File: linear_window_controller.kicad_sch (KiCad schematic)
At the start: 85 parts, among them J1 Motor 2, J2 Motor 1, J3 Motor 4, J4 Motor 3, J5 edge_psu_connector_64p, J9 Control, P1 ESP32 USB, SW2 Service, SW3 Service, SW4 Service, SW5 Service, SW6 Service, SW7 Service, U1 TSOP384xx, U10 TPS56220x, U2 DRV8874, U3 DRV8874, U4 DRV8874, U5 DRV8874, U6 PCF8574APWRG4, U8 ESP32-S3-WROOM-1-N16R2

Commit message: Finish most of the routing, add DM9051 fast ethernet controller
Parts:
- removed DS2: OLED-128O064D, iotta_footprints:OLED_0.96'_SSD1306_Folded, symbol Display_Graphic:OLED-128O064D
- added C20, C22, C27, C28, C33, C35: 22u, Capacitor_SMD:C_0603_1608Metric, symbol Device:C
- added C21, C23, C24, C26, C29, C30, C31, C32, C34, C36, C37, C45, C46: 100n, Capacitor_SMD:C_0603_1608Metric, symbol Device:C
- added C47: 1u, Capacitor_SMD:C_0603_1608Metric, symbol Device:C
- added D3, D4, D5, D8: SS14, Diode_SMD:D_SMA, symbol Diode:SS14
- added D6, D7: LED, LED_SMD:LED_0603_1608Metric, symbol Device:LED
- added DIS1: OLED_128x64, iotta_footprints:OLED_128x64_Module, symbol iotta:OLED_128x64
- added J6: ATX-24 (Molex 39-28-1243), Connector_Molex:Molex_Mini-Fit_Jr_5566-24A_2x12_P4.20mm_Vertical, symbol Connector:ATX-24
- added J7: Link-PP_LPJ0135GDNL, iotta_footprints:LinkPP_LPJ0135GDNL, symbol iotta:Link-PP_LPJ0135GDNL
- added J8: EXT_LED, Connector_PinSocket_2.54mm:PinSocket_1x03_P2.54mm_Vertical, symbol Connector_Generic:Conn_01x03
- added L2: FB0805/600R/2A, symbol Device:L_Ferrite_Small
- added P2: ESP32 USB, Connector_USB:USB_C_Receptacle_Palconn_UTC16-G, symbol Connector:USB_C_Receptacle_USB2.0_14P
- added Q1, Q2: BC817-40(SOT23), Package_TO_SOT_SMD:SOT-23, symbol MicroGw_prj:Q_NPN_BEC
- added Q3: BSS138, Package_TO_SOT_SMD:SOT-23, symbol Transistor_FET:BSS138
- added R27: 0, Resistor_SMD:R_0603_1608Metric, symbol Device:R
- added R28, R31, R32: 1k, Resistor_SMD:R_0603_1608Metric, symbol MicroGw_prj:R
- added R29, R30: 220, Resistor_SMD:R_0603_1608Metric, symbol MicroGw_prj:R
- added R33, R45, R46, R47, R48, R49, R50: 10k, Resistor_SMD:R_0603_1608Metric, symbol Device:R
- added R34: 100, Resistor_SMD:R_0603_1608Metric, symbol MicroGw_prj:R
- added R35, R36: 100, Resistor_SMD:R_0603_1608Metric, symbol Device:R
- added R37: 6k8, Resistor_SMD:R_0603_1608Metric, symbol Device:R
- added R38, R39, R44, R51: 300, Resistor_SMD:R_0603_1608Metric, symbol Device:R
- added R40, R41, R42, R43: 49.9, Resistor_SMD:R_0603_1608Metric, symbol Device:R
- added SW1: PGM, Button_Switch_SMD:SW_SPST_B3U-1000P, symbol Switch:SW_Push
- added U11: CP2102N-A01-GQFN24, Package_DFN_QFN:QFN-24-1EP_4x4mm_P0.5mm_EP2.6x2.6mm, symbol Interface_USB:CP2102N-A01-GQFN24
- added U12: 93LCxxAxxOT, Package_TO_SOT_SMD:SOT-23-6, symbol Memory_EEPROM:93LCxxAxxOT
- added U13: DM9051, Package_DFN_QFN:QFN-32-1EP_5x5mm_P0.5mm_EP3.3x3.3mm_ThermalVias, symbol iotta_v6:DM9051
- added Y1: 25MHz YXC X322525MOB4SI, Crystal:Crystal_SMD_3225-4Pin_3.2x2.5mm, symbol Device:Crystal_GND24
- F1: footprint Fuse:Fuseholder_Cylinder-5x20mm_Schurter_0031_8201_Horizontal_Open -> Fuse:Fuseholder_Clip-6.3x32mm_Littelfuse_102_122_Inline_P34.21x7.62mm_D1.98mm_Horizontal
- J5: value edge_psu_connector_64p -> Amphenol 10053363-200LF; footprint iotta_footprints_v6:Amphenol_10053363-200LF_WingTAT ER64BGFBK_Compatible -> iotta_footprints_v6:Amphenol_10053363-200LF_WingTAT ER64BGFBK_Compatible_BOTTOM
- P1: symbol Connector:USB_C_Plug_USB2.0 -> Connector:USB_C_Receptacle_USB2.0_14P
- SW6: now not fitted
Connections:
- net +12V_UNFUSED: now also J6.10 (+12V), J6.11 (+12V)
- net +3.3V: now also D1.2 (A), D2.2 (A), U1.3 (Vs), C26.2, C27.2, C28.2, C29.2, C30.2, C31.2, DIS1.2 (GND), J8.2 (Pin_2), L2.1, R33.2, R38.2, R39.2, R44.2, R45.2, R47.2, R48.2, R49.2, U12.6 (VCC), U13.15 (VDD33), U13.21 (VDD33), U13.29 (VDD33), U13.9 (TEST3); no longer R2.2, R3.2
- net A_DWN: now also SW5.2, U6.17 (P5); no longer SW3.2, U6.19 (P6)
- net A_UP: now also SW4.2, U6.16 (P4); no longer SW2.2, U6.20 (P7)
- net BTN_FUNC: now also U6.10 (P0); no longer U6.12 (P2)
- net B_DWN: now also SW3.2, U6.20 (P7); no longer SW5.2, U6.17 (P5)
- net B_UP: now also SW2.2, U6.19 (P6); no longer SW4.2, U6.16 (P4)
- net DRV1_IN1: now also U8.29 (SPIIO7/GPIO36/FSPICLK/SUBSPICLK)
- net DRV1_IN2: now also U8.28 (SPIIO6/GPIO35/FSPID/SUBSPID)
- net DRV1_IPROPI: now also U8.39 (GPIO1/TOUCH1/ADC1_CH0)
- net DRV2_IN1: now also U8.24 (GPIO47/SPICLK_P/SUBSPICLK_P_DIFF)
- net DRV2_IN2: now also U8.23 (GPIO21)
- net DRV2_IPROPI: now also U8.18 (GPIO10/TOUCH10/ADC1_CH9/FSPICS0/FSPIIO4/SUBSPICS0)
- net DRV3_IN1: now also U8.19 (GPIO11/TOUCH11/ADC2_CH0/FSPID/FSPIIO5/SUBSPID)
- net DRV3_IN2: now also U8.20 (GPIO12/TOUCH12/ADC2_CH1/FSPICLK/FSPIIO6/SUBSPICLK)
- net DRV3_IPROPI: now also U8.17 (GPIO9/TOUCH9/ADC1_CH8/FSPIHD/SUBSPIHD)
- net DRV4_IN1: now also U8.10 (GPIO17/U1TXD/ADC2_CH6)
- net DRV4_IN2: now also U8.11 (GPIO18/U1RXD/ADC2_CH7/CLK_OUT3)
- net DRV4_IPROPI: now also U8.15 (GPIO3/TOUCH3/ADC1_CH2)
- net GND: now also P1.A1 (GND), P1.A12 (GND), P1.B1 (GND), P1.B12 (GND), P1.S1 (SHIELD), U1.2 (GND), U8.1 (GND), U8.40 (GND), U8.41 (GND), C20.2, C21.2, C22.2, C23.2, C24.2, C26.1, C27.1, C28.1, C29.1, C30.1, C31.1, C32.1, C33.1, C34.1, C35.2, C36.1, C37.1, C45.2, C46.2, C47.2, DIS1.1 (VCC), J6.15 (GND), J6.17 (GND), J6.18 (GND), J6.19 (GND), J6.24 (GND), J6.3 (GND), J6.5 (GND), J6.7 (GND), P2.A1 (GND), P2.A12 (GND), P2.B1 (GND), P2.B12 (GND), P2.S1 (SHIELD), Q3.2 (S), R27.2, R37.2, R46.2, R50.1, R51.2, SW1.1, U11.2 (GND), U11.25 (GND), U12.2 (GND), U13.22 (TEST2), U13.32 (AGND), U13.33 (VSS), U13.5 (AGND), Y1.2, Y1.4; no longer J5.A27 (ADDR)
- net LED_F1: now also R3.1, U6.11 (P1), R35.2; no longer D1.1 (K), U6.10 (P0)
- net LED_F2: now also R2.1, U6.12 (P2), R36.2; no longer D2.1 (K), U6.11 (P1)
- net PS_OK: now also D7.2 (A), J6.8 (PWR_OK)
- net PS_ON: now also J6.16 (PS_ON#), Q3.3 (D)
- net SCL: now also U8.8 (GPIO15/U0RTS/ADC2_CH4/XTAL_32K_P), DIS1.3 (SCL), R48.1
- net SDA: now also U8.9 (GPIO16/U0CTS/ADC2_CH5/XTAL_32K_N), DIS1.4 (SDA), R49.1
- net ~{DRV1_FAULT}: now also U8.25 (GPIO48/SPICLK_N/SUBSPICLK_N_DIFF)
- net ~{DRV2_FAULT}: now also U8.22 (GPIO14/TOUCH14/ADC2_CH3/FSPIWP/FSPIDQS/SUBSPIWP)
- net ~{DRV3_FAULT}: now also U8.21 (GPIO13/TOUCH13/ADC2_CH2/FSPIQ/FSPIIO7/SUBSPIQ)
- net ~{DRV4_FAULT}: now also U8.12 (GPIO8/TOUCH8/ADC1_CH7/SUBSPICS1)
- net ~{DRV_SLEEP}: now also U8.26 (GPIO45)
- net ESPUSB-: now reaches U8.13 (GPIO19/U1RTS/ADC2_CH8/CLK_OUT2/USB_D-)
- net ESPUSB-: now also P1.A7 (D-), P1.B7 (D-)
- net ESPUSB+: now reaches U8.14 (GPIO20/U1CTS/ADC2_CH9/CLK_OUT1/USB_D+)
- net ESPUSB+: now also P1.A6 (D+), P1.B6 (D+)
- net ~{IOEX1_INT}: now reaches U8.16 (GPIO46)
- net ~{IOEX1_INT}: now also U6.1 (~{INT})
- net ~{ESP_PGM}: now reaches U8.27 (GPIO0/BOOT)
- net ~{ESP_PGM}: now also R34.1
- net ESP_EN: now reaches U8.3 (EN)
- net ESP_EN: now also C24.1, Q1.3 (C), R33.1
- net LAN_MISO: now reaches U8.30 (SPIDQS/GPIO37/FSPIQ/SUBSPIQ)
- net LAN_MISO: now also U13.20 (SPI_MISO)
- net LAN_MOSI: now reaches U8.31 (GPIO38/FSPIWP/SUBSPIWP)
- net LAN_MOSI: now also U13.19 (SPI_MOSI)
- net LAN_CK: now reaches U8.32 (MTCK/GPIO39/CLK_OUT3/SUBSPICS1)
- net LAN_CK: now also U13.18 (SPI_CK)
- net LAN_CSN: now reaches U8.33 (MTDO/GPIO40/CLK_OUT2)
- net LAN_CSN: now also U13.17 (SPI_CSN)
- net ~{LAN_INT}: now reaches U8.34 (MTDI/GPIO41/CLK_OUT1)
- net ~{LAN_INT}: now also U13.24 (INT)
- net IR_REMOTE: now reaches U8.35 (MTMS/GPIO42)
- net IR_REMOTE: now also U1.1 (OUT)
- net U0RXD: now reaches U8.36 (U0RXD/GPIO44/CLK_OUT2)
- net U0RXD: now also R30.2
- net U0TXD: now reaches U8.37 (U0TXD/GPIO43/CLK_OUT1)
- net U0TXD: now also R29.2
- net PS_ENABLE: now reaches U8.38 (GPIO2/TOUCH2/ADC1_CH1)
- net PS_ENABLE: now also Q3.1 (G), R50.2
- net at P1.A4 (VBUS), P1.A9 (VBUS), P1.B4 (VBUS)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: now also D4.2 (A)
- net +12P renamed DCDC_IN
- net DCDC_IN: now also D3.1 (K), D4.1 (K), D5.1 (K), D8.1 (K); no longer J5.B28 (+12VSB), R1.2
- new net: C20.1, C21.1, R28.1, U11.5 (VIO), U11.6 (VDD)
- new net: R28.2, U11.9 (~{RSTb})
- new net: Q2.3 (C), R34.2, SW1.2
- new net: C36.2, U13.30 (X2), Y1.1
- new net: C37.2, U13.31 (X1), Y1.3
- new net: C46.1, R42.1, R43.1
- new net: D2.1 (K), R2.2
- new net: J7.1 (RD+), R40.2, U13.3 (RX+)
- new net: J7.11 (LED1_A), R38.1
- new net: J7.13 (LED2_A), R39.1
- new net: J7.3 (RD-), R41.2, U13.4 (RX-)
- new net: J7.4 (TD+), R42.2, U13.6 (TX+)
- new net: J7.6 (TD-), R43.2, U13.7 (TX-)
- new net: Q2.1 (B), R32.2
- new net: R37.1, U13.1 (BGRES)
- new net: R46.1, U13.14 (WOL)
- new net: C45.1, R40.1, R41.1
- new net: C47.1, R47.1, U13.27 (RSTB)
- new net: D7.1 (K), R51.1
- new net: D6.2 (A), R44.1
- new net: D1.1 (K), R3.2
- new net: J5.A27 (ADDR), R27.1
- new net: J8.3 (Pin_3), R36.1
- new net: Q1.1 (B), R31.2
- new net: J8.1 (Pin_1), R35.1
- new net +3.3v: J6.1 (+3.3V), J6.12 (+3.3V), J6.13 (+3.3V), J6.2 (+3.3V)
- new net +5VSB: D8.2 (A), J6.9 (+5VSB)
- new net +5v: J6.21 (+5V), J6.22 (+5V), J6.23 (+5V), J6.4 (+5V), J6.6 (+5V)
- new net +V12SB: D3.2 (A), J5.B28 (+12VSB), R1.2
- new net -12V: J6.14 (-12V)
- new net AVDD: C32.2, C33.2, C34.2, C35.1, J7.2 (CT), J7.5 (CT), L2.2, U13.2 (AVDD), U13.8 (AVDD)
- new net DTR: Q2.2 (E), R31.1, U11.23 (DTR)
- new net EECK: R45.1, U12.4 (CLK), U13.12 (EECK)
- new net EECS: U12.5 (CS), U13.13 (EECS)
- new net EEDIO: U12.1 (DO), U12.3 (DI), U13.11 (EEDIO)
- new net LAN_ACT: J7.12 (LED1_K), U13.25 (LINKLED)
- new net LAN_FDX: D6.1 (K), U13.16 (FXLED)
- new net LAN_SPEED: J7.14 (LED2_K), U13.26 (SPDLED)
- new net RTS: Q1.2 (E), R32.1, U11.19 (RTS)
- new net RXD: R29.1, U11.20 (RXD)
- new net TXD: R30.1, U11.21 (TXD)
- new net USB_D+: P2.A6 (D+), P2.B6 (D+), U11.3 (D+)
- new net USB_D-: P2.A7 (D-), P2.B7 (D-), U11.4 (D-)
- new net VBUS: C22.1, C23.1, D5.2 (A), P2.A4 (VBUS), P2.A9 (VBUS), P2.B4 (VBUS), P2.B9 (VBUS), U11.7 (REGIN), U11.8 (VBUS)
- no-connect marks 0 -> 13
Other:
- note added: "0"
- note added: "1"
- note added: "1.8V"
- note added: "3.3V"
- note added: "Auto program"
- note added: "Booting Mode"
- note added: "Bootstrapping Pins Settings"
- note added: "DTR RTS->EN IO0"
- note added: "Debugging Log on U0TXD During Booting"
- note added: "Default"
- note added: "Don't-care"
- note added: "Download Boot"
- note added: "EECK strap: INT low active"
- note added: "Falling-edge:Input"
- note added: "Falling-edge:Output"
- note added: "GPIO0"
- note added: "GPIO0:"
- note added: "GPIO12/MTDI"
- note added: "GPIO15/MTDO"
- note added: "GPIO2"
- note added: "GPIO2:"
- note added: "GPIO4:"
- note added: "GPIO5"
- note added: "GPIO5:"
- note added: "Internal Bootstrapping Resistors"
- note added: "MTDI/GPIO12:"
- note added: "MTDO/GPIO15:"
- note added: "Pin"
- note added: "Pull-Down"
- note added: "Pull-Up"
- note added: "Rising-edge:Input"
- note added: "Rising-edge:Output"
- note added: "SPI Flash Boot"
- note added: "Timing of SDIO Slave"
- note added: "U0TXD Silent"
- note added: "U0TXD Toggling"
- note added: "VCC/GND POLARISATIONS BOTH EXIST"
- note added: "Voltage of Internal LDO(VDD_SDIO)"
- note added: "WOL strap: INT Push-Pull"
- moved on the sheet: C17, C42, C43, C47, D1, D2, J9, L6, R2, R24, R3, R6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

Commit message: Finalize routing and cleanup. Change DCDC to TPS562200 Add some more things (e.g. power monitoring LEDs) Update some partno's in BOM
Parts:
- removed U10: TPS56220x, Package_TO_SOT_SMD:SOT-23-6, symbol iotta_v6:TPS56220x
- added D10: Vsb, LED_SMD:LED_0603_1608Metric, symbol Device:LED
- added D11: VCC, LED_SMD:LED_0603_1608Metric, symbol Device:LED
- added D9: Vmain, LED_SMD:LED_0603_1608Metric, symbol Device:LED
- added J10, J11: DCDC_IN, Connector_PinHeader_2.54mm:PinHeader_1x01_P2.54mm_Vertical, symbol Connector:Conn_01x01_Pin
- added J12: VCC, Connector_PinHeader_2.54mm:PinHeader_1x01_P2.54mm_Vertical, symbol Connector:Conn_01x01_Pin
- added J14: PANEL_BTN, Connector_PinHeader_2.54mm:PinHeader_1x06_P2.54mm_Vertical, symbol Connector_Generic:Conn_01x06
- added R52, R53: 1k, Resistor_SMD:R_0603_1608Metric, symbol MicroGw_prj:R
- added R54: 300, Resistor_SMD:R_0603_1608Metric, symbol Device:R
- added R55: 470, Resistor_SMD:R_0603_1608Metric, symbol Device:R
- added R56: 100, Resistor_SMD:R_0603_1608Metric, symbol Device:R
- added U9: TPS562200, Package_TO_SOT_SMD:SOT-23-6, symbol Regulator_Switching:TPS562200
- C36, C37: value 100n -> 18p
- D7: value LED -> PSOK
- J5: LCSC# (none) -> C5173350
- J6: LCSC# (none) -> C114088
- J8: value EXT_LED -> PANEL_LED
- L2: footprint (none) -> Inductor_SMD:L_0805_2012Metric
- L6: value 4.7µ -> 2.2µ; LCSC (none) -> C135262; Manuf (none) -> SXN; PartNr (none) -> SMNR4020-2.2UH
- P1: LCSC# (none) -> C2927039; Manuf (none) -> DEALON; PartNr (none) -> USB-TYPE-C-019
- P2: value ESP32 USB -> CONSOLE; LCSC# (none) -> C2927039; Manuf (none) -> DEALON; PartNr (none) -> USB-TYPE-C-019
- R24: value 100k -> 33k
- R24: value 22k -> 10k
- U12: value 93LCxxAxxOT -> 93LC46BT-E/OT
- Y1: LCSC# (none) -> C9006
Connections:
- net POT+ is gone; now on net +3.3V: J1.5 (Pin_5), J2.5 (Pin_5), J3.5 (Pin_5), J4.5 (Pin_5)
- net POTCOM is gone; now on net GND: J1.3 (Pin_3), J2.3 (Pin_3), J3.3 (Pin_3), J4.3 (Pin_3)
- net +12V_UNFUSED: now also D9.2 (A)
- net +3.3V: now also D11.2 (A), J12.1 (Pin_1)
- net A_DWN: now also J14.3 (Pin_3)
- net A_UP: now also J14.1 (Pin_1)
- net BTN_FUNC: now also U6.14 (P3); no longer U6.10 (P0)
- net BTN_SVC: now also U6.10 (P0); no longer U6.14 (P3)
- net B_DWN: now also J14.6 (Pin_6)
- net B_UP: now also J14.4 (Pin_4)
- net DCDC_IN: now also D10.2 (A), J10.1 (Pin_1), U9.3 (VIN); no longer D4.1 (K)
- net GND: now also J14.2 (Pin_2), J14.5 (Pin_5), R52.2, R53.2, R54.2, R55.2, R56.2, U9.1 (GND)
- net at R6.2: now also U9.5 (EN)
- net at C42.2, L6.1: now also U9.2 (SW)
- net at C42.1: now also U9.6 (VBST)
- net at R24.2, R24.2: now also U9.4 (VFB)
- net at P2.A5 (CC1): now also P2.B5 (CC2), R52.1
- net at P1.A5 (CC1): now also P1.B5 (CC2), R53.1
- net +3.3v: no longer names the net of J6.1 (+3.3V), J6.12 (+3.3V), J6.13 (+3.3V), J6.2 (+3.3V)
- net +5v: no longer names the net of J6.21 (+5V), J6.22 (+5V), J6.23 (+5V), J6.4 (+5V), J6.6 (+5V)
- net -12V: no longer names the net of J6.14 (-12V)
- new net: D9.1 (K), R54.1
- new net: D4.1 (K), J11.1 (Pin_1)
- new net: D11.1 (K), R56.1
- new net: D10.1 (K), R55.1
- no-connect marks 13 -> 17
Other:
- note added: "Vout = 0,765 * (1 + R1/R2)"
- note removed: "Vout = 0,6 * (1 + R1/R2)"
- moved on the sheet: C17, C20, C21, C22, C23, C26, C27, C28, C29, C30, C31, C32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

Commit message: Update schematic layout and fully update BOM for production
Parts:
- C11, C14, C3, C6: LCSC# (none) -> C7471886; Manuf (none) -> KNSCHA; PartNr (none) -> 189RV0024
- C20, C21, C22, C23: PartCmnt Generic X7R -> (none)
- D1, D10, D9: LCSC# (none) -> C84263; Manuf (none) -> Foshan; PartCmnt (none) -> Red; PartNr (none) -> NCD0603R1
- D2, D6, D7: LCSC# (none) -> C7429914; Manuf (none) -> Foshan; PartCmnt (none) -> Green; PartNr (none) -> NCD0603G3
- D3, D4, D5, D8: LCSC# (none) -> C2480; Manuf (none) -> MDD; PartNr (none) -> SS14
- DIS1, H1, H2, H3, H4, J10, J11, J12, J14, J7, J8, JP1, JP2, JP3, JP4, U1: now not fitted
- F1: LCSC# (none) -> C206903; Manuf (none) -> Littelfuse; PartCmnt (none) -> 2x!; PartNr (none) -> 01220088Z
- J1: LCSC# (none) -> C5349549; Manuf (none) -> MAX; PartCmnt (none) -> One part for J1/2; PartNr (none) -> MAX MX127S-3.5-10P-GN01-Cu-Y-A; now not fitted
- J2: LCSC# (none) -> C5349549; Manuf (none) -> MAX; PartCmnt (none) -> One part for J1/2; PartNr (none) -> MAX MX127S-3.5-10P-GN01-Cu-Y-A
- J3: LCSC# (none) -> C5349549; Manuf (none) -> MAX; PartCmnt (none) -> One part for J3/J4; PartNr (none) -> MAX MX127S-3.5-10P-GN01-Cu-Y-A; now not fitted
- J4: LCSC# (none) -> C5349549; Manuf (none) -> MAX; PartCmnt (none) -> One part for J3/J4; PartNr (none) -> MAX MX127S-3.5-10P-GN01-Cu-Y-A
- J5: Manuf (none) -> WingTAT; PartNr (none) -> ER64BGFBK
- J9: LCSC# (none) -> C5349547; Manuf (none) -> MAX; PartNr (none) -> MX127S-3.5-06P-GN01-Cu-Y-A
- L2: LCSC# (none) -> C524530; Manuf (none) -> Murata; PartNr (none) -> BLM21AG601BH1D
- L6: LCSC C135262 -> (none); LCSC# (none) -> C135262
- Q1, Q2: LCSC# (none) -> C52801; Manuf ON Semi -> Nexperia; PartNr BC817-16LT3G -> BC817-40,215
- Q3: LCSC# (none) -> C40912; Manuf (none) -> DIODES; PartNr (none) -> BSS138-7-F
- R28, R29, R30, R31, R32, R34, R52, R53: Manuf Kemet / Generic -> (none)
- SW1: LCSC# (none) -> C231329
- SW2, SW3, SW4, SW5, SW7: LCSC# (none) -> C2888508; Manuf XKB -> BZCN; PartNr (none) -> TSC015A04818B
- SW6: LCSC# (none) -> C2888508; Manuf XKB -> BZCN; PartNr (none) -> TSC015A04818B; now fitted
- U11: LCSC# (none) -> C969151; PartNr CP2102N-A01-GQFN24 -> CP2102N-A02-GQFN24R
- U12: LCSC# (none) -> C2061604; Manuf (none) -> Microchip; PartNr (none) -> 93LC46BT-E/OT
- U13: LCSC# (none) -> C113756; Manuf (none) -> DAVICOM; PartNr (none) -> DM9051NP
- U2, U3, U4, U5: LCSC# (none) -> C1855818; Manuf (none) -> TI; PartNr (none) -> DRV8874PWPR
- U6: LCSC# (none) -> C5310793; Manuf (none) -> HGSEMI; PartNr (none) -> PCF8574AM/TR
- U8: LCSC# (none) -> C2913205; Manuf (none) -> Espressif; PartNr (none) -> ESP32-S3-WROOM-1-N16R2
- U9: Manuf (none) -> TI; PartNr (none) -> TPS562200DDCR
- Y1: Manuf (none) -> YXC; PartNr (none) -> X322525MOB4SI
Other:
- note added: "ATX"
- note added: "Fast Ethernet"
- note added: "MCU"
- note added: "Motor Control"
- note added: "Native USB"
- note added: "PSU"
- note added: "Power indicators"
- note added: "Serial USB Console / PGM"
- note added: "Server PSU"
- note added: "UI"
- note added: "USB I/F"
- note removed: "Raming IO lijnen General DIO 2 I2C peripheral bus PSU DO 1 PS_ON AI 1 Imonitor AI 1 PS_OK DI 1 FAULT/INTERRUPT DIO 2 PMBus 4x Motor control DO 2 EN/PH DO 1 !SLEEP DI 1 !FAULT AI 1 IPropi AO 1 VRef (via external I2C dac?) Extra radio (optional) DIO 4 SPI (or other) DI 1 Int DIO 1 Optional User input DI 1 Infra red DI 4 Knopbediening Total needed IO's Analog 6 Digital 33"
- moved on the sheet: C1, C10, C11, C12, C13, C14, C15, C16, C17, C18, C19, C2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

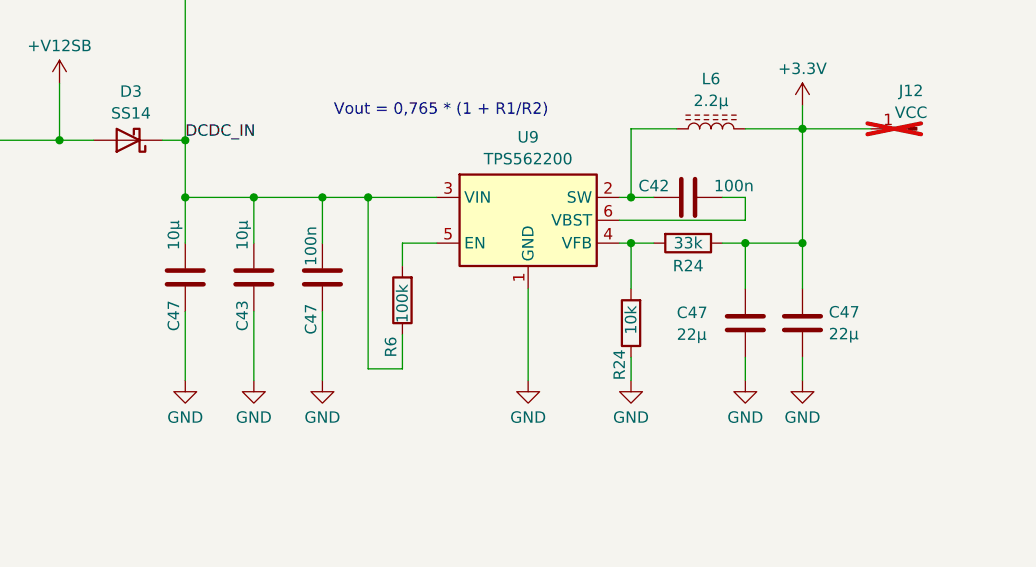
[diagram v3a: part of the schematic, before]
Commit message: Update edge connector orientation (correct bottom mount)
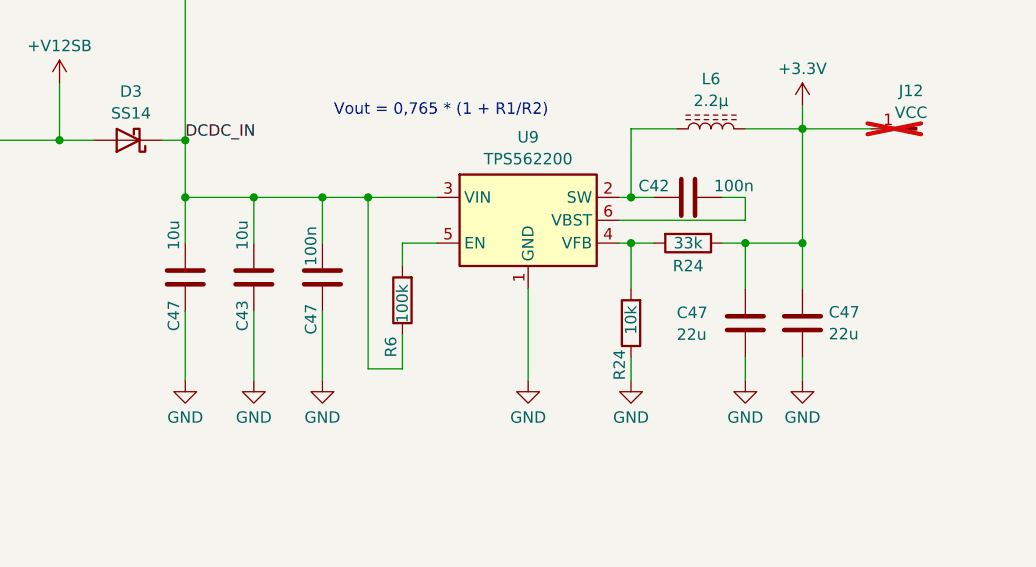
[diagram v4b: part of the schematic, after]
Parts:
- C11, C14, C3, C6: LCSC Part # (none) -> C7471886; LCSC# C7471886 -> (none)
- C43, C47: value 10µ -> 10u
- C47: value 22µ -> 22u
- D1, D10, D9: LCSC Part # (none) -> C84263; LCSC# C84263 -> (none)
- D11: LCSC Part # (none) -> C84263; Manuf (none) -> Foshan; PartCmnt (none) -> Red; PartNr (none) -> NCD0603R1
- D2, D6, D7: LCSC Part # (none) -> C7429914; LCSC# C7429914 -> (none)
- D3, D4, D5, D8: LCSC Part # (none) -> C2480; LCSC# C2480 -> (none)
- F1: LCSC Part # (none) -> C206903; LCSC# C206903 -> (none)
- J1, J2, J3, J4: LCSC Part # (none) -> C5349549; LCSC# C5349549 -> (none)
- J5: LCSC Part # (none) -> C5173350; LCSC# C5173350 -> (none)
- J6: LCSC Part # (none) -> C114088; LCSC# C114088 -> (none)
- J9: LCSC Part # (none) -> C5349547; LCSC# C5349547 -> (none)
- L2: LCSC Part # (none) -> C524530; LCSC# C524530 -> (none)
- L6: LCSC Part # (none) -> C135262; LCSC# C135262 -> (none)
- P1, P2: LCSC Part # (none) -> C2927039; LCSC# C2927039 -> (none)
- Q1, Q2: LCSC Part # (none) -> C52801; LCSC# C52801 -> (none)
- Q3: LCSC Part # (none) -> C40912; LCSC# C40912 -> (none)
- SW1: LCSC Part # (none) -> C231329; LCSC# C231329 -> (none)
- SW2, SW3, SW4, SW5, SW6, SW7: LCSC Part # (none) -> C2888508; LCSC# C2888508 -> (none)
- U11: LCSC Part # (none) -> C969151; LCSC# C969151 -> (none); PartNr CP2102N-A02-GQFN24R -> CP2102N-A02-GQFN24R
- U12: LCSC Part # (none) -> C2061604; LCSC# C2061604 -> (none)
- U13: LCSC Part # (none) -> C113756; LCSC# C113756 -> (none)
- U2, U3, U4, U5: LCSC Part # (none) -> C1855818; LCSC# C1855818 -> (none)
- U6: LCSC Part # (none) -> C94361; LCSC# C5310793 -> (none); Manuf HGSEMI -> TI; PartNr PCF8574AM/TR -> PCF8574APWR
- U8: LCSC Part # (none) -> C2913205; LCSC# C2913205 -> (none)
- U9: LCSC Part # (none) -> C49757; LCSC# C49757 -> (none)
- Y1: LCSC Part # (none) -> C9006; LCSC# C9006 -> (none)

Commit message: Add TMP100 and LIS3DH sensors, update board layout, teardrops
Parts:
- removed SW6: Service, Button_Switch_SMD:SW_SPST_TL3305B, symbol Switch:SW_Push
- added C25, C44: 100n, Capacitor_SMD:C_0603_1608Metric, symbol Device:C
- added H5: 12V MAIN, MountingHole:MountingHole_3.2mm_M3_Pad_Via, symbol Mechanical:MountingHole_Pad
- added J13: GND, TestPoint:TestPoint_Plated_Hole_D2.0mm, symbol Connector:Conn_01x01_Pin
- added Q4: BSS138, Package_TO_SOT_SMD:SOT-23, symbol Transistor_FET:BSS138
- added R57: 10k, Resistor_SMD:R_0603_1608Metric, symbol Device:R
- added U10: TMP100, Package_TO_SOT_SMD:SOT-23-6, symbol Sensor_Temperature:TMP100
- added U7: LIS3DH, Package_LGA:LGA-16_3x3mm_P0.5mm_LayoutBorder3x5y, symbol Sensor_Motion:LIS3DH
- DIS1, H1, H2, H3, J1, J10, J12, J14, J3, J7, J8, JP1, JP2, JP3, JP4, U1: now fitted; now left out of the parts list
- H4: value MountingHole -> GND; symbol Mechanical:MountingHole -> Mechanical:MountingHole_Pad; now fitted; now left out of the parts list
- J11: value DCDC_IN -> VBus; now fitted; now left out of the parts list
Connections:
- net +12V_UNFUSED: now also H5.1
- net +3.3V: now also C25.1, C44.1, U10.4 (V+), U7.1 (VDD_IO), U7.14 (VDD), U7.8 (CS)
- net +V12SB: now also J5.A28 (+12VSB); no longer J5.B28 (+12VSB)
- net GND: now also H4.1, J5.B30 (+12VSB_GND/RTN), C25.2, C44.2, J13.1 (Pin_1), Q4.2 (S), R57.1, U10.2 (GND), U10.3 (ADD1), U10.5 (ADD0), U7.10 (GND), U7.12 (GND), U7.5 (GND); no longer J5.A30 (+12VSB_GND/RTN)
- net PS_IMONITOR: now also J5.A31 (IMonitor); no longer J5.B31 (IMonitor)
- net PS_INTERRUPT: now also J5.A27 (PS_INTTERUPT); no longer J5.B27 (PS_INTTERUPT)
- net PS_OK: now also J5.A30 (PS_OK), Q4.1 (G), R57.2; no longer J5.B30 (PS_OK)
- net PS_ON: now also J5.A32 (PS_ON); no longer J5.B32 (PS_ON)
- net PS_SCL: now also J5.B32 (SCL); no longer J5.A32 (SCL)
- net PS_SDA: now also J5.B31 (SDA); no longer J5.A31 (SDA)
- net SCL: now also U10.1 (SCL), U7.4 (SCL/SPC)
- net SDA: now also U10.6 (SDA), U7.6 (SDA/SDI/SDO)
- net at R1.1: now also J5.A29 (PRESENT#); no longer J5.B29 (PRESENT#)
- net at R27.1: now also J5.B27 (ADDR); no longer J5.A27 (ADDR)
- net BTN_SVC renamed ~{nPS_OK}
- net ~{nPS_OK}: now also Q4.3 (D)
- no-connect marks 17 -> 23
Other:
- moved on the sheet: C18, C19, C24, R33, R48, R49, U8

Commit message: Update schematic with (resistor) values and informative text
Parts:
- removed U10: TMP100, Package_TO_SOT_SMD:SOT-23-6, symbol Sensor_Temperature:TMP100
- added JP5: PMBUS_DA, Jumper:SolderJumper-2_P1.3mm_Open_TrianglePad1.0x1.5mm, symbol Jumper:SolderJumper_2_Open
- added JP6: PMBUS_CL, Jumper:SolderJumper-2_P1.3mm_Open_TrianglePad1.0x1.5mm, symbol Jumper:SolderJumper_2_Open
- added U10: TMP112AIDRLR, Package_TO_SOT_SMD:SOT-563, symbol Sensor_Temperature:TMP112xxDRL
- J2, J4, J9, R27: now left out of the parts list
- L6: value 2.2µ -> 4.7µ; LCSC Part # C135262 -> C135270; PartNr SMNR4020-2.2UH -> SMNR4030-4R7MT
- P1, P2: Alternative (none) -> C2982555
- R10, R15, R20, R25: value TBD -> ${r_ipropi}
- R11, R12, R17, R22: value TBD -> 10k
- R13, R18, R23, R7: value TBD -> ${vrefupper}
- R14, R19, R24, R8: value TBD -> ${vreflower}
- U6: value PCF8574APWRG4 -> PCF8574APWRG4
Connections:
- net +3.3V: now also U10.5 (V+)
- net GND: now also U10.2 (GND), U10.4 (ADD0)
- net PS_SCL: now also JP6.1 (A)
- net PS_SDA: now also JP5.1 (A)
- net SCL: now also JP6.2 (B), U10.1 (SCL)
- net SDA: now also JP5.2 (B), U10.6 (SDA)
- no-connect marks 23 -> 24
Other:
- note added: "EECK strap (hi): INT low active"
- note added: "PotPWR"
- note added: "WOL strap (low): INT Push-Pull"
- note removed: "EECK strap: INT low active"
- note removed: "WOL strap: INT Push-Pull"
- moved on the sheet: C44, D1, D2, D8, J8, Q3, Q4, R1, R2, R27, R3, R35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
